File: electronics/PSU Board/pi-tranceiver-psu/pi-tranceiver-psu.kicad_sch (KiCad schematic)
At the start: 60 parts, among them IC1 LTC4368IMS-2#PBF, IC2 LM2679S-ADJ_NOPB, J1 Wago PCB 2 Pole, J10 JST 01x02, J11 JST 01x04, J12 JST 01x02, J2 Wago PCB 2 Pole, J3 Wago PCB 2 Pole, J4 Wago PCB 2 Pole, J5 Wago PCB 2 Pole, J6 Wago PCB 2 Pole, J7 JST 01x02, J8 JST 01x02, J9 JST 01x02, Q1 DMT6002LPS-13, Q2 DMT6002LPS-13, Q3 Q_PMOS_GDS, Q4 BC547, Q5 BC547, SW1 SW_Push, U1 AMS1117-5.0, U2 AMS1117-5.0

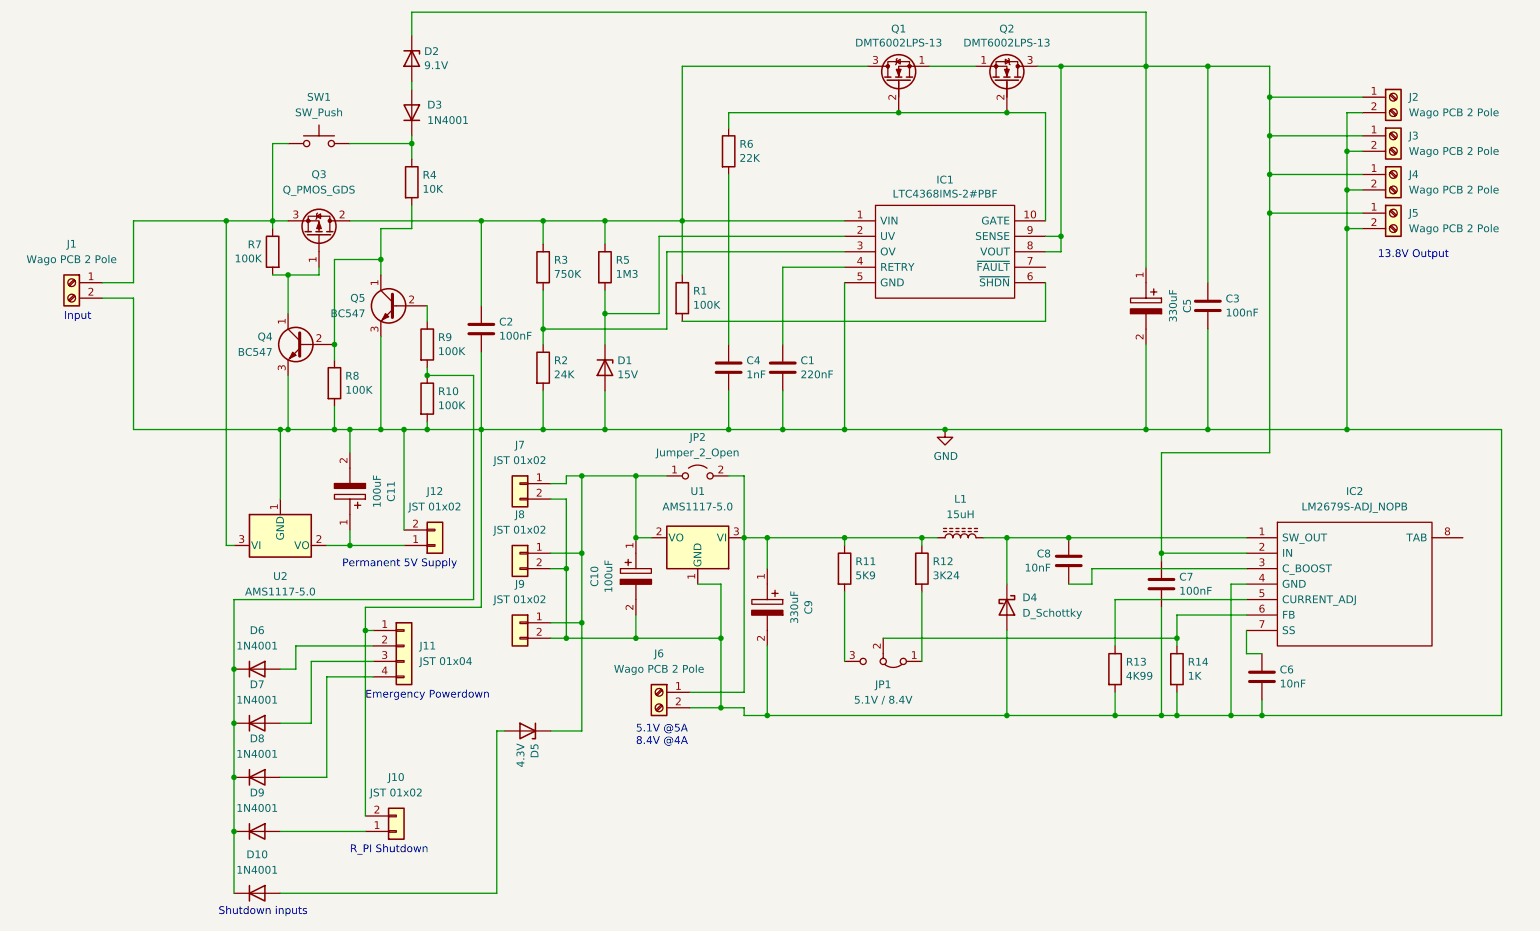
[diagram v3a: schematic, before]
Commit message: Added connects to parts list and footprint
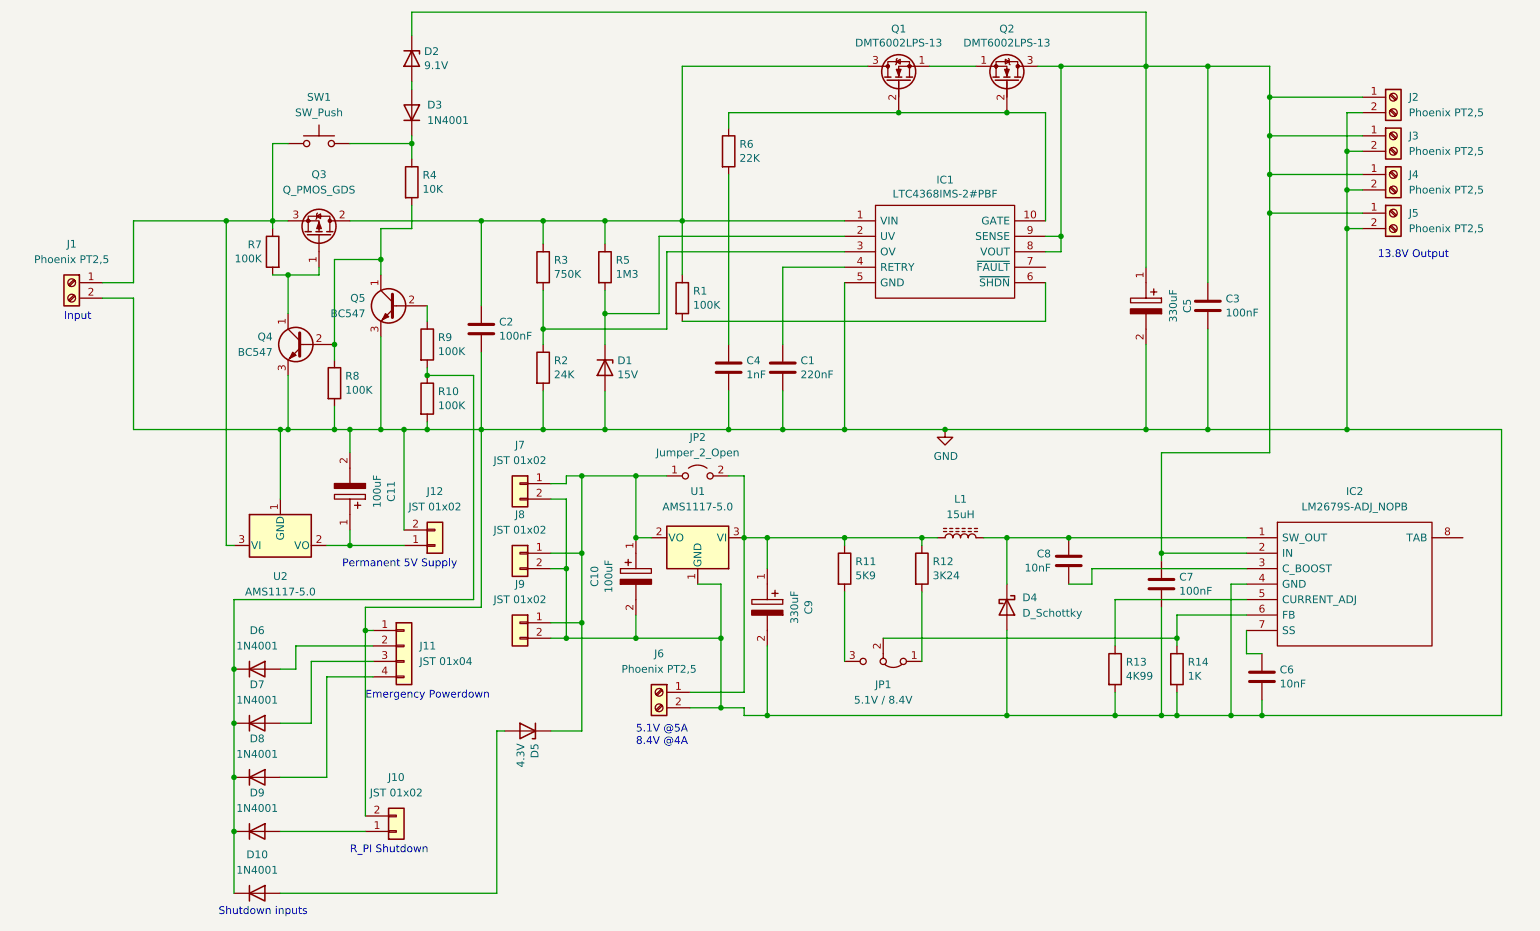
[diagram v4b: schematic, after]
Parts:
- J1, J2, J3, J4, J5, J6: value Wago PCB 2 Pole -> Phoenix PT2,5; footprint (none) -> TerminalBlock_Phoenix:TerminalBlock_Phoenix_PT-1,5-2-5.0-H_1x02_P5.00mm_Horizontal
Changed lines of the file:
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@@
       (effects (font (size 1.27 1.27)) (justify left))
     )
-    (property "Value" "Wago PCB 2 Pole" (id 1) (at 250.19 33.0199 0)
-      (effects (font (size 1.27 1.27)) (justify left))
-    )
-    (property "Footprint" "" (id 2) (at 247.65 30.48 0)
+    (property "Value" "Phoenix PT2,5" (id 1) (at 250.19 33.0199 0)
+      (effects (font (size 1.27 1.27)) (justify left))
+    )
+    (property "Footprint" "TerminalBlock_Phoenix:TerminalBlock_Phoenix_PT-1,5-2-5.0-H_1x02_P5.00mm_Horizontal" (id 2) (at 247.65 30.48 0)
       (effects (font (size 1.27 1.27)) hide)
     )
@@
       (effects (font (size 1.27 1.27)) (justify left))
     )
-    (property "Value" "Wago PCB 2 Pole" (id 1) (at 250.19 52.0699 0)
-      (effects (font (size 1.27 1.27)) (justify left))
-    )
-    (property "Footprint" "" (id 2) (at 247.65 49.53 0)
+    (property "Value" "Phoenix PT2,5" (id 1) (at 250.19 52.0699 0)
+      (effects (font (size 1.27 1.27)) (justify left))
+    )
+    (property "Footprint" "TerminalBlock_Phoenix:TerminalBlock_Phoenix_PT-1,5-2-5.0-H_1x02_P5.00mm_Horizontal" (id 2) (at 247.65 49.53 0)
       (effects (font (size 1.27 1.27)) hide)
     )
@@
       (effects (font (size 1.27 1.27)) (justify left))
     )
-    (property "Value" "Wago PCB 2 Pole" (id 1) (at 250.19 45.7199 0)
-      (effects (font (size 1.27 1.27)) (justify left))
-    )
-    (property "Footprint" "" (id 2) (at 247.65 43.18 0)
+    (property "Value" "Phoenix PT2,5" (id 1) (at 250.19 45.7199 0)
+      (effects (font (size 1.27 1.27)) (justify left))
+    )
+    (property "Footprint" "TerminalBlock_Phoenix:TerminalBlock_Phoenix_PT-1,5-2-5.0-H_1x02_P5.00mm_Horizontal" (id 2) (at 247.65 43.18 0)
       (effects (font (size 1.27 1.27)) hide)
     )
@@
     (in_bom yes) (on_board yes) (fields_autoplaced)
     (property "Reference" "J1" (id 0) (at 30.48 54.61 0))
-    (property "Value" "Wago PCB 2 Pole" (id 1) (at 30.48 57.15 0))
-    (property "Footprint" "" (id 2) (at 30.48 60.96 0)
+    (property "Value" "Phoenix PT2,5" (id 1) (at 30.48 57.15 0))
+    (property "Footprint" "TerminalBlock_Phoenix:TerminalBlock_Phoenix_PT-1,5-2-5.0-H_1x02_P5.00mm_Horizontal" (id 2) (at 30.48 60.96 0)
       (effects (font (size 1.27 1.27)) hide)
     )
@@
       (effects (font (size 1.27 1.27)) (justify left))
     )
-    (property "Value" "Wago PCB 2 Pole" (id 1) (at 250.19 39.3699 0)
-      (effects (font (size 1.27 1.27)) (justify left))
-    )
-    (property "Footprint" "" (id 2) (at 247.65 36.83 0)
+    (property "Value" "Phoenix PT2,5" (id 1) (at 250.19 39.3699 0)
+      (effects (font (size 1.27 1.27)) (justify left))
+    )
+    (property "Footprint" "TerminalBlock_Phoenix:TerminalBlock_Phoenix_PT-1,5-2-5.0-H_1x02_P5.00mm_Horizontal" (id 2) (at 247.65 36.83 0)
       (effects (font (size 1.27 1.27)) hide)
     )
@@
     (in_bom yes) (on_board yes) (fields_autoplaced)
     (property "Reference" "J6" (id 0) (at 127 121.92 0))
-    (property "Value" "Wago PCB 2 Pole" (id 1) (at 127 124.46 0))
-    (property "Footprint" "" (id 2) (at 127 128.27 0)
+    (property "Value" "Phoenix PT2,5" (id 1) (at 127 124.46 0))
+    (property "Footprint" "TerminalBlock_Phoenix:TerminalBlock_Phoenix_PT-1,5-2-5.0-H_1x02_P5.00mm_Horizontal" (id 2) (at 127 128.27 0)
       (effects (font (size 1.27 1.27)) hide)
     )
@@
     )
     (path "/bb8199de-6f9e-4429-ac37-73d54de1c446"
-      (reference "J1") (unit 1) (value "Wago PCB 2 Pole") (footprint "")
+      (reference "J1") (unit 1) (value "Phoenix PT2,5") (footprint "TerminalBlock_Phoenix:TerminalBlock_Phoenix_PT-1,5-2-5.0-H_1x02_P5.00mm_Horizontal")
     )
     (path "/20236ddc-98ed-4719-ac21-8a7df8203fc2"
-      (reference "J2") (unit 1) (value "Wago PCB 2 Pole") (footprint "")
+      (reference "J2") (unit 1) (value "Phoenix PT2,5") (footprint "TerminalBlock_Phoenix:TerminalBlock_Phoenix_PT-1,5-2-5.0-H_1x02_P5.00mm_Horizontal")
     )
     (path "/c20f008a-5d4f-41de-a370-47cfbe150ac9"
-      (reference "J3") (unit 1) (value "Wago PCB 2 Pole") (footprint "")
+      (reference "J3") (unit 1) (value "Phoenix PT2,5") (footprint "TerminalBlock_Phoenix:TerminalBlock_Phoenix_PT-1,5-2-5.0-H_1x02_P5.00mm_Horizontal")
     )
     (path "/b7c05c36-1785-43e0-a6a8-d26455336680"
-      (reference "J4") (unit 1) (value "Wago PCB 2 Pole") (footprint "")
+      (reference "J4") (unit 1) (value "Phoenix PT2,5") (footprint "TerminalBlock_Phoenix:TerminalBlock_Phoenix_PT-1,5-2-5.0-H_1x02_P5.00mm_Horizontal")
     )
     (path "/7d36ae10-6d9b-4816-898b-9020de9a8bc3"
-      (reference "J5") (unit 1) (value "Wago PCB 2 Pole") (footprint "")
+      (reference "J5") (unit 1) (value "Phoenix PT2,5") (footprint "TerminalBlock_Phoenix:TerminalBlock_Phoenix_PT-1,5-2-5.0-H_1x02_P5.00mm_Horizontal")
     )
     (path "/c98301f7-3c31-4d95-9696-37a894f6a7b9"
-      (reference "J6") (unit 1) (value "Wago PCB 2 Pole") (footprint "")
+      (reference "J6") (unit 1) (value "Phoenix PT2,5") (footprint "TerminalBlock_Phoenix:TerminalBlock_Phoenix_PT-1,5-2-5.0-H_1x02_P5.00mm_Horizontal")
     )
     (path "/55a2db0b-8149-47f9-a74e-47f1a3e26820"
